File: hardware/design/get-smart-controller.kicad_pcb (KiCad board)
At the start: 2 copper layers, 44.2 x 44.9 mm, 20 parts, among them J1 USB_B_Micro, J2 BOOT, J3 UART, U1 ESP32-S3-WROOM-1, U2 AMS1117-3.3, U3 Ai-Thinker-Ra-02

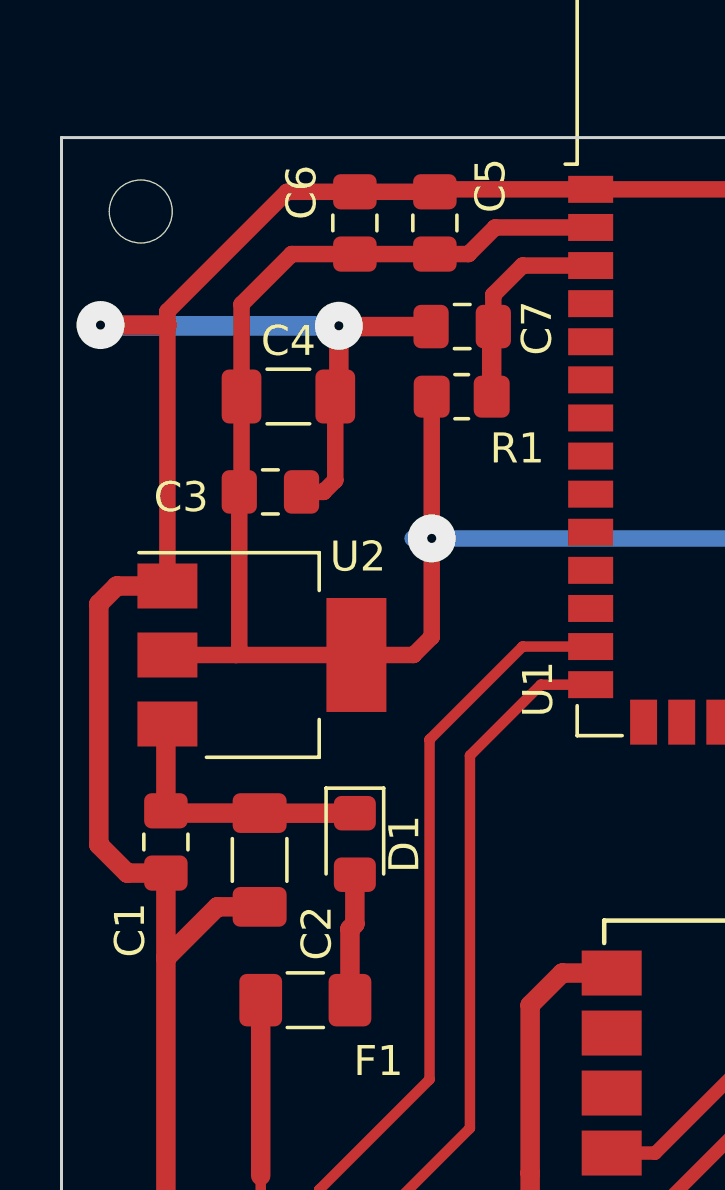
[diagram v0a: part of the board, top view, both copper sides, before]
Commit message: Updated PCB with holes
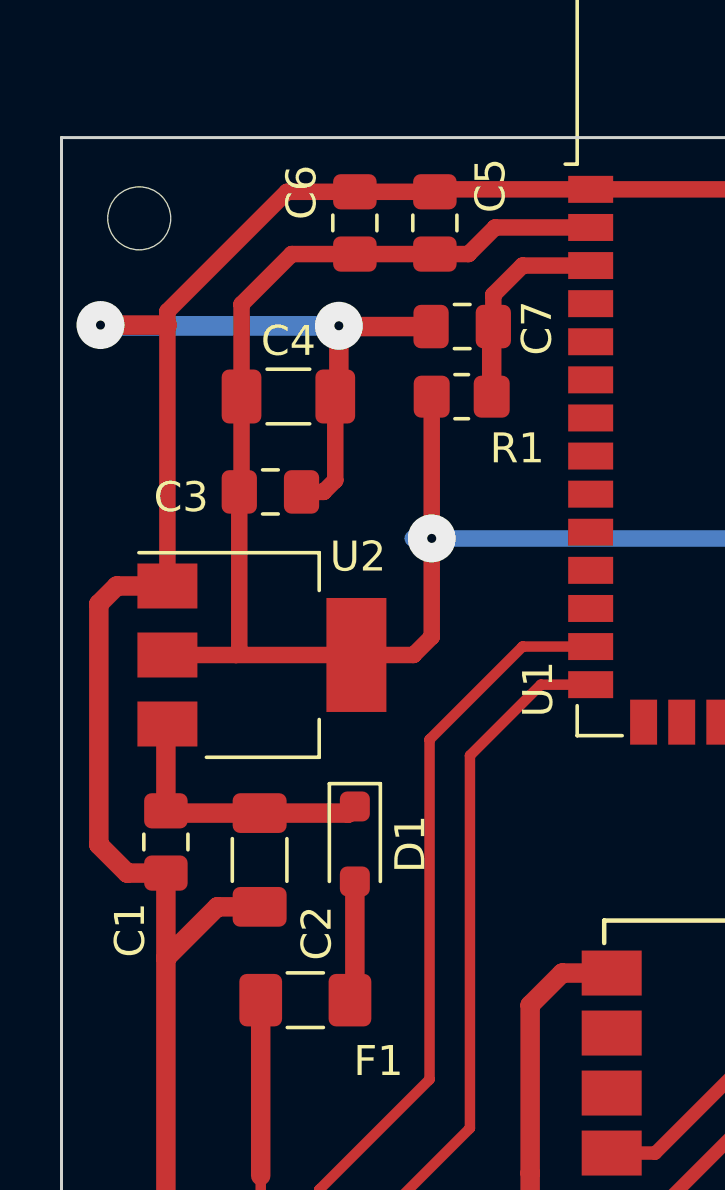
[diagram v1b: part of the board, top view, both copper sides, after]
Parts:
- D1: value 1N5819 -> SS14; footprint Diode_SMD:D_0805_2012Metric_Pad1.15x1.40mm_HandSolder -> Diode_SMD:D_SOD-323_HandSoldering
- moved H1 0.23 mm to (77.6, 62.3)
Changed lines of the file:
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@@
 		(allow_soldermask_bridges_in_footprints no)
 		(pcbplotparams
-			(layerselection 0x0000000_7fffffff)
-			(plot_on_all_layers_selection 0x0001000_00000000)
+			(layerselection 0x0000080_7fffffff)
+			(plot_on_all_layers_selection 0x0001200_00000000)
 			(disableapertmacros no)
 			(usegerberextensions no)
@@
 		)
 	)
-	(footprint "Diode_SMD:D_0805_2012Metric_Pad1.15x1.40mm_HandSolder"
+	(footprint "Diode_SMD:D_SOD-323_HandSoldering"
 		(layer "F.Cu")
 		(at 84.836 83.185 -90)
-		(descr "Diode SMD 0805 (2012 Metric), square (rectangular) end terminal, IPC_7351 nominal, (Body size source: https://docs.google.com/spreadsheets/d/1BsfQQcO9C6DZCsRaXUlFlo91Tg2WpOkGARC1WS5S8t0/edit?usp=sharing), generated with kicad-footprint-generator")
-		(tags "diode handsolder")
+		(descr "SOD-323")
+		(tags "SOD-323")
 		(property "Reference" "D1"
-			(at 0 -1.65 -90)
+			(at 0 -1.85 -90)
 			(layer "F.SilkS")
 			(effects
@@
 			)
 		)
-		(property "Value" "1N5819"
-			(at 0 1.65 -90)
+		(property "Value" "SS14"
+			(at 0.1 1.9 -90)
 			(layer "F.Fab")
 			(effects
@@
 			)
 		)
-		(property "Footprint" "Diode_SMD:D_0805_2012Metric_Pad1.15x1.40mm_HandSolder"
+		(property "Footprint" "Diode_SMD:D_SOD-323_HandSoldering"
 			(at 0 0 -90)
 			(unlocked yes)
@@
 		(attr smd)
 		(fp_line
-			(start -1.86 0.96)
-			(end 1 0.96)
+			(start -2.01 0.85)
+			(end 1.25 0.85)
 			(stroke
 				(width 0.12)
@@
 		)
 		(fp_line
-			(start -1.86 -0.96)
-			(end -1.86 0.96)
+			(start -2.01 -0.85)
+			(end -2.01 0.85)
 			(stroke
 				(width 0.12)
@@
 		)
 		(fp_line
-			(start 1 -0.96)
-			(end -1.86 -0.96)
+			(start -2.01 -0.85)
+			(end 1.25 -0.85)
 			(stroke
 				(width 0.12)
@@
 		)
 		(fp_line
-			(start -1.85 0.95)
-			(end -1.85 -0.95)
+			(start -2 0.95)
+			(end 2 0.95)
 			(stroke
 				(width 0.05)
@@
 		)
 		(fp_line
-			(start 1.85 0.95)
-			(end -1.85 0.95)
+			(start -2 -0.95)
+			(end -2 0.95)
 			(stroke
 				(width 0.05)
@@
 		)
 		(fp_line
-			(start -1.85 -0.95)
-			(end 1.85 -0.95)
+			(start -2 -0.95)
+			(end 2 -0.95)
 			(stroke
 				(width 0.05)
@@
 		)
 		(fp_line
-			(start 1.85 -0.95)
-			(end 1.85 0.95)
+			(start 2 -0.95)
+			(end 2 0.95)
 			(stroke
 				(width 0.05)
@@
 		)
 		(fp_line
-			(start -1 0.6)
-			(end 1 0.6)
+			(start -0.9 0.7)
+			(end -0.9 -0.7)
+			(stroke
+				(width 0.1)
+				(type solid)
+			)
+			(layer "F.Fab")
+		)
+		(fp_line
+			(start 0.9 0.7)
+			(end -0.9 0.7)
+			(stroke
+				(width 0.1)
+				(type solid)
+			)
+			(layer "F.Fab")
+		)
+		(fp_line
+			(start 0.2 0.35)
+			(end -0.3 0)
+			(stroke
+				(width 0.1)
+				(type solid)
+			)
+			(layer "F.Fab")
+		)
+		(fp_line
+			(start -0.3 0)
+			(end -0.5 0)
 			(stroke
 				(width 0.1)
@@
 		)
 		(fp_line
-			(start 1 0.6)
-			(end 1 -0.6)
+			(start -0.3 0)
+			(end 0.2 -0.35)
 			(stroke
 				(width 0.1)
@@
 		)
 		(fp_line
-			(start -1 -0.3)
-			(end -1 0.6)
+			(start 0.2 0)
+			(end 0.45 0)
 			(stroke
 				(width 0.1)
@@
 		)
 		(fp_line
-			(start -0.7 -0.6)
-			(end -1 -0.3)
+			(start -0.3 -0.35)
+			(end -0.3 0.35)
 			(stroke
 				(width 0.1)
@@
 		)
 		(fp_line
-			(start 1 -0.6)
-			(end -0.7 -0.6)
+			(start 0.2 -0.35)
+			(end 0.2 0.35)
+			(stroke
+				(width 0.1)
+				(type solid)
+			)
+			(layer "F.Fab")
+		)
+		(fp_line
+			(start -0.9 -0.7)
+			(end 0.9 -0.7)
+			(stroke
+				(width 0.1)
+				(type solid)
+			)
+			(layer "F.Fab")
+		)
+		(fp_line
+			(start 0.9 -0.7)
+			(end 0.9 0.7)
 			(stroke
 				(width 0.1)
@@
 		)
 		(fp_text user "${REFERENCE}"
-			(at 0 0 -90)
+			(at 0 -1.85 -90)
 			(layer "F.Fab")
 			(effects
 				(font
-					(size 0.5 0.5)
-					(thickness 0.08)
+					(size 1 1)
+					(thickness 0.15)
 				)
 			)
 		)
 		(pad "1" smd roundrect
-			(at -1.025 0 270)
-			(size 1.15 1.4)
+			(at -1.25 0 270)
+			(size 1 1)
 			(layers "F.Cu" "F.Paste" "F.Mask")
-			(roundrect_rratio 0.2173913043)
+			(roundrect_rratio 0.25)
 			(net 2 "+5V")
 			(pinfunction "K")
@@
 		)
 		(pad "2" smd roundrect
-			(at 1.025 0 270)
-			(size 1.15 1.4)
+			(at 1.25 0 270)
+			(size 1 1)
 			(layers "F.Cu" "F.Paste" "F.Mask")
-			(roundrect_rratio 0.2173913043)
+			(roundrect_rratio 0.25)
 			(net 5 "Net-(D1-A)")
 			(pinfunction "A")
 			(pintype "passive")
 		)
-		(model "${KICAD6_3DMODEL_DIR}/Diode_SMD.3dshapes/D_0805_2012Metric.wrl"
+		(model "${KICAD6_3DMODEL_DIR}/Diode_SMD.3dshapes/D_SOD-323.wrl"
 			(offset
 				(xyz 0 0 0)
@@
 	(footprint "MountingHole:MountingHole_2.1mm"
 		(layer "F.Cu")
-		(at 77.6986 62.103)
+		(at 77.6478 62.3316)
 		(descr "Mounting Hole 2.1mm, no annular")
 		(tags "mounting hole 2.1mm no annular")
@@
 	)
 	(segment
+		(start 81.661 82.1559)
+		(end 84.6151 82.1559)
+		(width 0.65)
+		(layer "F.Cu")
+		(net 2)
+	)
+	(segment
 		(start 78.6118 82.1559)
 		(end 78.5368 82.0809)
@@
 	)
 	(segment
-		(start 84.836 82.16)
-		(end 81.6651 82.16)
+		(start 84.6151 82.1559)
+		(end 84.836 81.935)
 		(width 0.65)
 		(layer "F.Cu")
@@
 	)
 	(segment
-		(start 84.836 85.852)
-		(end 84.836 84.21)
-		(width 0.65)
-		(layer "F.Cu")
-		(net 5)
-	)
-	(segment
-		(start 84.6725 86.0155)
-		(end 84.836 85.852)
+		(start 84.836 84.435)
+		(end 84.836 88.2285)
 		(width 0.65)
 		(layer "F.Cu")
@@
 	)
 	(segment
-		(start 84.6725 88.392)
-		(end 84.6725 86.0155)
+		(start 84.836 88.2285)
+		(end 84.6725 88.392)
 		(width 0.65)
 		(layer "F.Cu")

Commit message: Add additional Ground path
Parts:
- removed H2: TestPoint_Plated_Hole_D2.0mm, TestPoint:TestPoint_Plated_Hole_D2.0mm
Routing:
- net GND: track 193.5 -> 207.9 mm

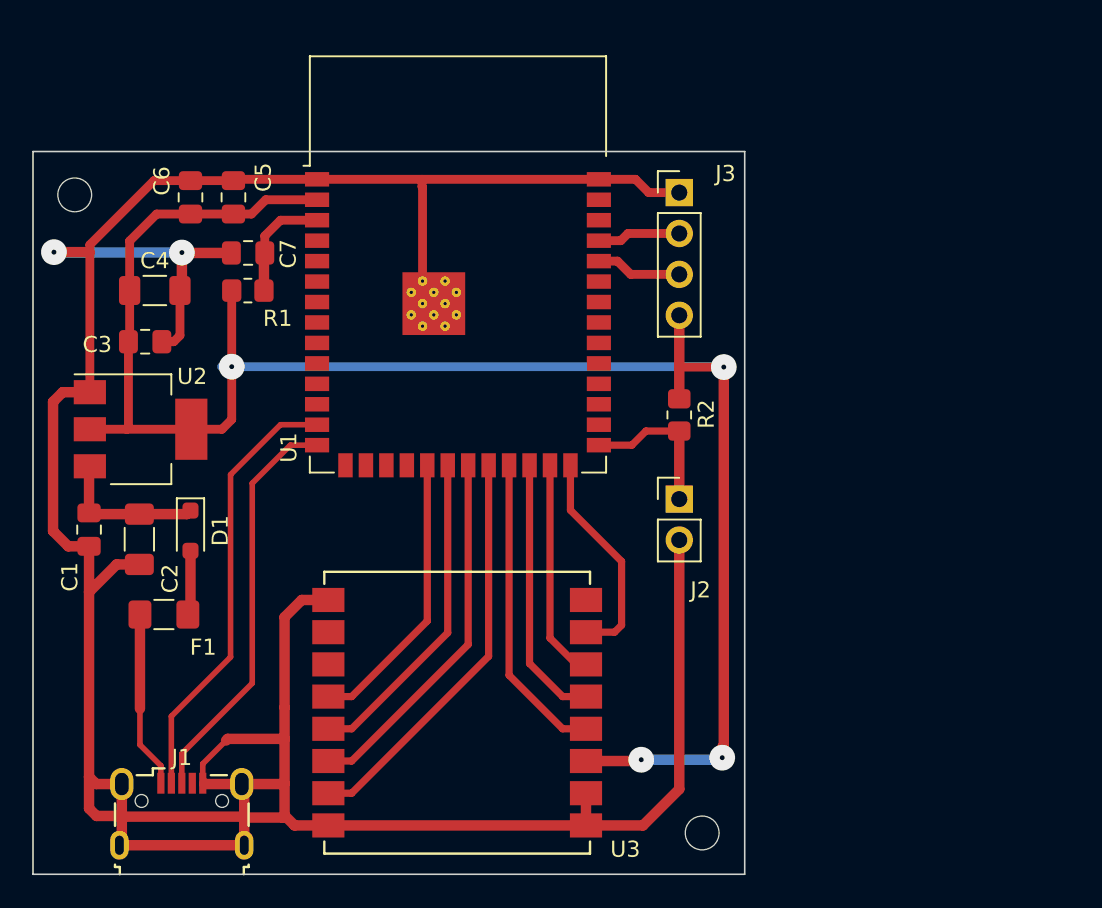
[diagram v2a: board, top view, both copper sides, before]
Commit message: Added RGB led, and fixed foorptint for USB Micro
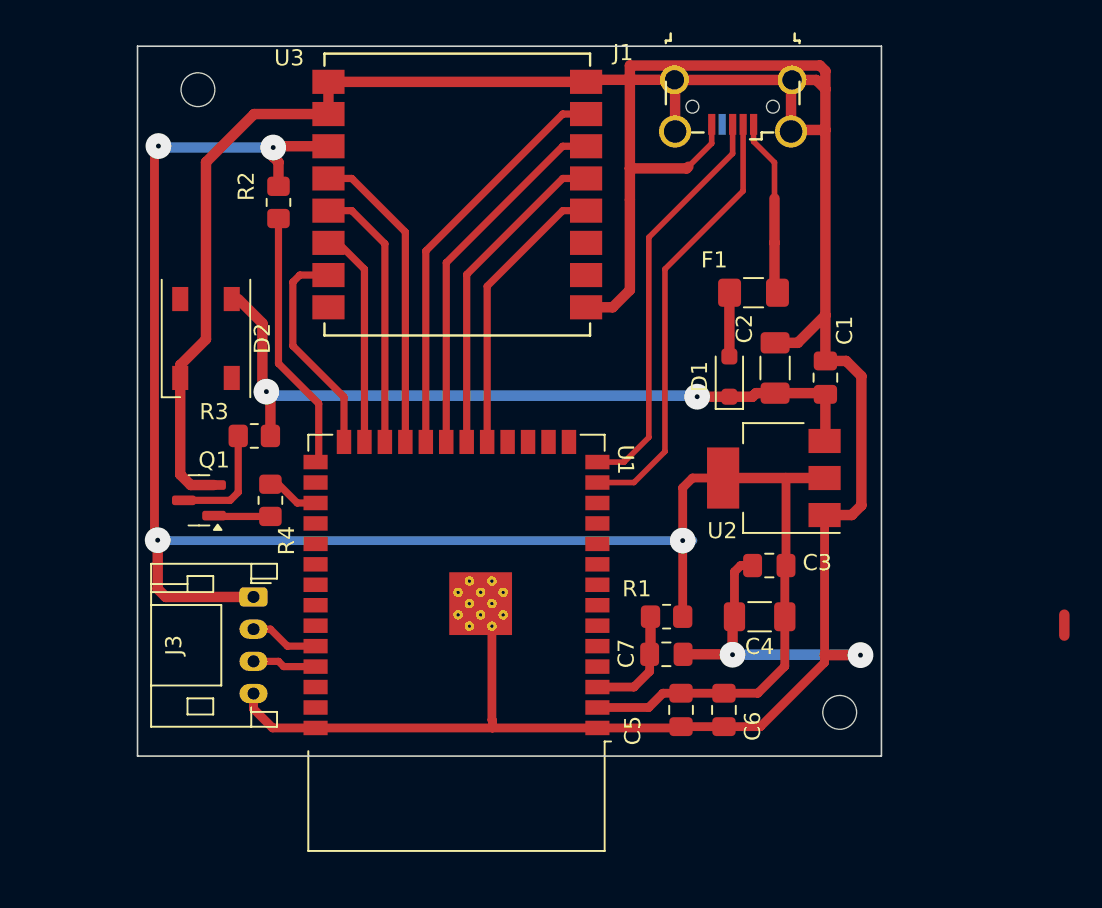
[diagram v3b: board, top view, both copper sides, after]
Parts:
- removed J2: BOOT, Connector_PinHeader_2.54mm:PinHeader_1x02_P2.54mm_Vertical
- added D2: SK6812, LED_SMD:LED_SK6812_PLCC4_5.0x5.0mm_P3.2mm, F.Cu at (85.8, 71.2)
- added Q1: MMBT3904, Package_TO_SOT_SMD:SOT-23, F.Cu at (85.4, 81.3)
- added R3: 1k, Resistor_SMD:R_0805_2012Metric_Pad1.20x1.40mm_HandSolder, F.Cu at (88.8, 77.3)
- added R4: 1k, Resistor_SMD:R_0805_2012Metric_Pad1.20x1.40mm_HandSolder, F.Cu at (89.8, 81.3)
- J1: footprint Connector_USB:USB_Micro-B_Wuerth_629105150521 -> Connector_USB:USB_Micro-B_Custom
- J3: footprint Connector_PinHeader_2.54mm:PinHeader_1x04_P2.54mm_Vertical -> Connector_JST:JST_PH_S4B-PH-K_1x04_P2.00mm_Horizontal
- moved H1 57.4 mm to (125.2, 94.5), turned to 180 degrees
- moved H3 55.8 mm to (85.3, 55.8), turned to 180 degrees
- moved J1 52.6 mm to (114.8, 57.9), turned to 180 degrees
- moved C1 46.7 mm to (124.3, 73.7), turned to 90 degrees
- moved C6 45.9 mm to (118.0, 94.3), turned to -90 degrees
- moved C4 42.7 mm to (120.2, 88.5), turned to 180 degrees
- moved C5 42.3 mm to (115.3, 94.3), turned to -90 degrees
- moved F1 41.7 mm to (119.8, 68.4), turned to 180 degrees
- moved C3 41.2 mm to (120.8, 85.3), turned to 180 degrees
- moved C2 40.9 mm to (121.1, 73.1), turned to 90 degrees
- moved U2 39.4 mm to (121.1, 79.9), turned to 180 degrees
- moved J3 36.5 mm to (88.8, 87.3), turned to -90 degrees
- moved C7 36.0 mm to (114.4, 90.9), turned to 0 degrees
- moved D1 34.8 mm to (118.3, 73.6), turned to 90 degrees
- moved R1 33.0 mm to (114.4, 88.5), turned to 180 degrees
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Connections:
- J3 pad 1: GND -> +3V3
- J3 pad 2: /TX -> /RX
- J3 pad 3: /RX -> /TX
- J3 pad 4: +3V3 -> GND
- U1 pad 29: unconnected-(U1-SPIIO7/GPIO36/FSPICLK/SUBSPICLK-Pad29) -> /RGB
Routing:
- net +5V: track 9.34 -> 47.2 mm, vias 0 -> 2
- net GND: track 207.9 -> 218.2 mm
- net +3V3: track 113.4 -> 121.6 mm
- net Net-(Q1-C): track 0.00 -> 7.08 mm
- net /BOOT: track 9.58 -> 16.2 mm
- net Net-(Q1-B): track 0.00 -> 3.52 mm
- net /RGB: track 0.00 -> 3.29 mm
- net (no net): track 0.00 -> 1.30 mm
- net /TX: track 5.18 -> 3.99 mm
- net /RX: track 5.33 -> 4.29 mm
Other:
- board size 44.2 x 44.9 mm -> 46.2 x 44.1 mm
